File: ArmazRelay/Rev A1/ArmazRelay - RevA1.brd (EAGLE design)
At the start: 70 x 30 mm, 5 parts, among them J1 22-05-7028-02, J2 MSTBA3, K1 MY2

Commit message: Update board
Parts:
- added CC1: CC-BY-NC-SA, cc-by-sa:CC-BY-NC-SA
- added T1: EXMACHINA-LOGO-NAME, exmachina:EXM-LOGO-BASELINE
- moved H1 1.50 mm to (15.0, 15.0)
- moved H2 1.50 mm to (55.0, 15.0)
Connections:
- new net +24V: J2.1, K1.9
- new net GND: J1.2, J2.3, K1.14
- new net SIG_IN: J2.2, K1.13
- new net SIG_OUT: J1.1, K1.5
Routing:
- net SIG_OUT: track 0.00 -> 42.2 mm
- net SIG_IN: track 0.00 -> 37.1 mm
- added copper zone on layer 1, net +24V
- added copper zone on layer 16, net GND
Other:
- board text added: "ArmazRelay RevA1"
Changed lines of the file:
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@@
 <setting verticaltext="up"/>
 </settings>
-<grid distance="1" unitdist="mm" unit="mm" style="lines" multiple="1" display="no" altdistance="0.5" altunitdist="mm" altunit="mm"/>
+<grid distance="1" unitdist="mm" unit="mm" style="lines" multiple="1" display="no" altdistance="0.1" altunitdist="mm" altunit="mm"/>
 <layers>
 <layer number="1" name="Top" color="4" fill="1" visible="yes" active="yes"/>
@@
 <wire x1="67" y1="30" x2="3" y2="30" width="0" layer="20"/>
 <wire x1="3" y1="30" x2="0" y2="27" width="0" layer="20" curve="90"/>
+<dimension x1="15" y1="15" x2="55" y2="15" x3="35" y3="-7" textsize="2.54" layer="48"/>
+<dimension x1="35" y1="15" x2="0" y2="15" x3="17.5" y3="34" textsize="2.54" layer="48"/>
+<dimension x1="55.5" y1="15" x2="55.5" y2="30" x3="87" y3="22.5" textsize="2.54" layer="48"/>
+<dimension x1="67" y1="30" x2="58" y2="0" x3="95" y3="15" textsize="2.54" layer="48" dtype="vertical"/>
+<dimension x1="0" y1="3" x2="70" y2="4" x3="35" y3="-14" textsize="2.54" layer="48" dtype="horizontal"/>
+<text x="57.6" y="22.4" size="1.27" layer="21">ArmazRelay
+RevA1</text>
 </plain>
 <attributes>
@@
 </autorouter>
 <elements>
-<element name="H1" library="holes" package="3,0" value="MOUNT-HOLE3.0" x="13.5" y="15"/>
-<element name="H2" library="holes" package="3,0" value="MOUNT-HOLE3.0" x="56.5" y="15"/>
+<element name="H1" library="holes" package="3,0" value="MOUNT-HOLE3.0" x="15" y="15"/>
+<element name="H2" library="holes" package="3,0" value="MOUNT-HOLE3.0" x="55" y="15"/>
 <element name="J1" library="con-molex" package="7395-02" value="22-05-7028-02" x="65" y="15" rot="R90">
 <attribute name="OC_FARNELL" value="9731601" x="65" y="15" size="1.778" layer="27" rot="R90" display="off"/>
@@
 </element>
 <element name="K1" library="rel-omron" package="PY08" value="MY2" x="35" y="15" rot="R90"/>
+<element name="CC1" library="cc-by-sa" package="CC-BY-NC-SA" value="CC-BY-NC-SA" x="15" y="26"/>
+<element name="T1" library="exmachina" package="EXM-LOGO-BASELINE" value="EXMACHINA-LOGO-NAME" x="54" y="25"/>
 </elements>
 <signals>
+<signal name="+24V">
+<contactref element="J2" pad="1"/>
+<contactref element="K1" pad="9"/>
+<polygon width="0.4064" layer="1">
+<vertex x="-15" y="45"/>
+<vertex x="103" y="45"/>
+<vertex x="103" y="-21"/>
+<vertex x="-15" y="-21"/>
+</polygon>
+</signal>
+<signal name="GND">
+<contactref element="J2" pad="3"/>
+<contactref element="J1" pad="2"/>
+<contactref element="K1" pad="14"/>
+<polygon width="0.4064" layer="16">
+<vertex x="-13" y="43"/>
+<vertex x="101" y="43"/>
+<vertex x="101" y="25"/>
+<vertex x="101" y="-20"/>
+<vertex x="59" y="-20"/>
+<vertex x="-13" y="-20"/>
+</polygon>
+</signal>
+<signal name="SIG_IN">
+<contactref element="J2" pad="2"/>
+<contactref element="K1" pad="13"/>
+<wire x1="7.08" y1="15" x2="4" y2="15" width="0.4064" layer="1"/>
+<wire x1="4" y1="15" x2="3" y2="14" width="0.4064" layer="1"/>
+<wire x1="3" y1="14" x2="3" y2="6" width="0.4064" layer="1"/>
+<wire x1="3" y1="6" x2="4" y2="5" width="0.4064" layer="1"/>
+<wire x1="4" y1="5" x2="23" y2="5" width="0.4064" layer="1"/>
+<wire x1="23" y1="5" x2="24.75" y2="6.75" width="0.4064" layer="1"/>
+<wire x1="24.75" y1="6.75" x2="24.75" y2="8.5" width="0.4064" layer="1"/>
+</signal>
+<signal name="SIG_OUT">
+<contactref element="J1" pad="1"/>
+<contactref element="K1" pad="5"/>
+<wire x1="35.15" y1="8.5" x2="35.15" y2="5.85" width="0.4064" layer="1"/>
+<wire x1="35.15" y1="5.85" x2="36" y2="5" width="0.4064" layer="1"/>
+<wire x1="36" y1="5" x2="59" y2="5" width="0.4064" layer="1"/>
+<wire x1="59" y1="5" x2="61" y2="7" width="0.4064" layer="1"/>
+<wire x1="61" y1="7" x2="61" y2="15" width="0.4064" layer="1"/>
+<wire x1="61" y1="15" x2="62.27" y2="16.27" width="0.4064" layer="1"/>
+<wire x1="62.27" y1="16.27" x2="65" y2="16.27" width="0.4064" layer="1"/>
+</signal>
 </signals>
 </board>
 </drawing>
+<compatibility>
+<note version="6.3" minversion="6.2.2" severity="warning">
+Since Version 6.2.2 text objects can contain more than one line,
+which will not be processed correctly with this version.
+</note>
+</compatibility>
 </eagle>

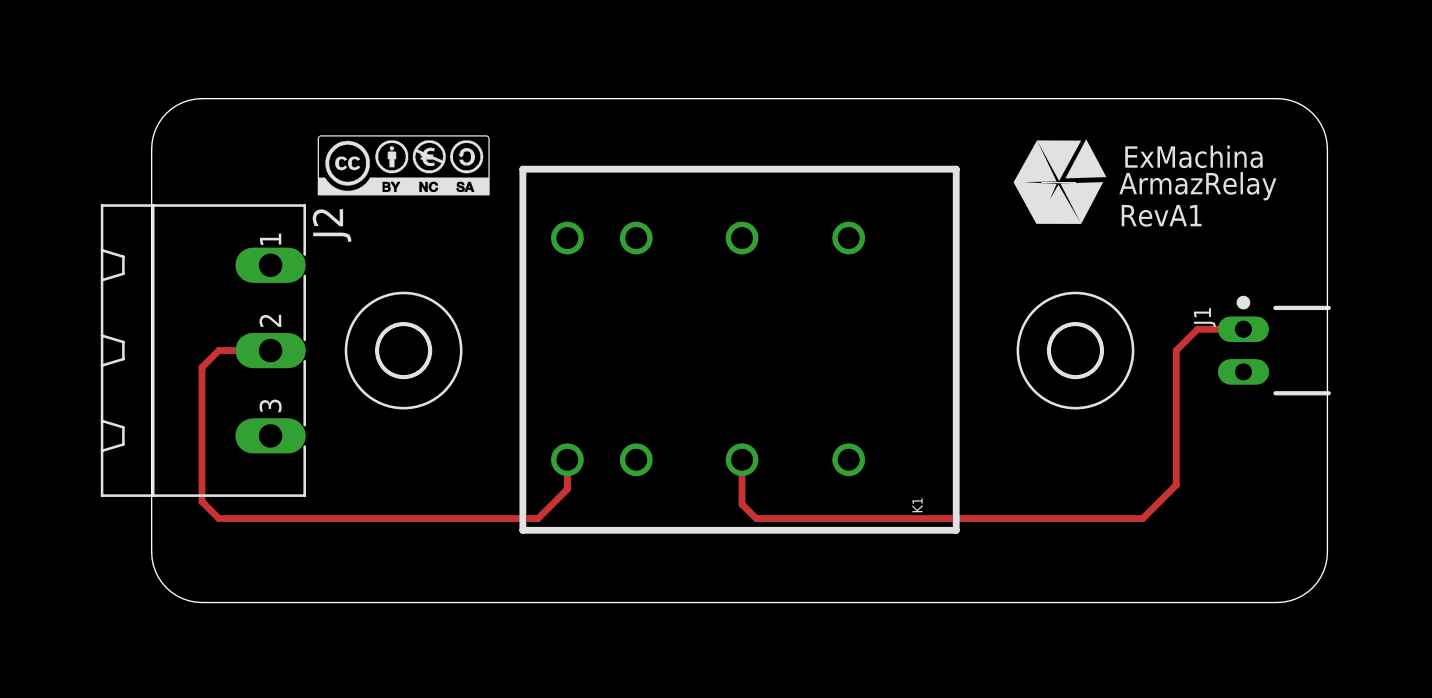
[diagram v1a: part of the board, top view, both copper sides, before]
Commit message: Add power connector and NC output
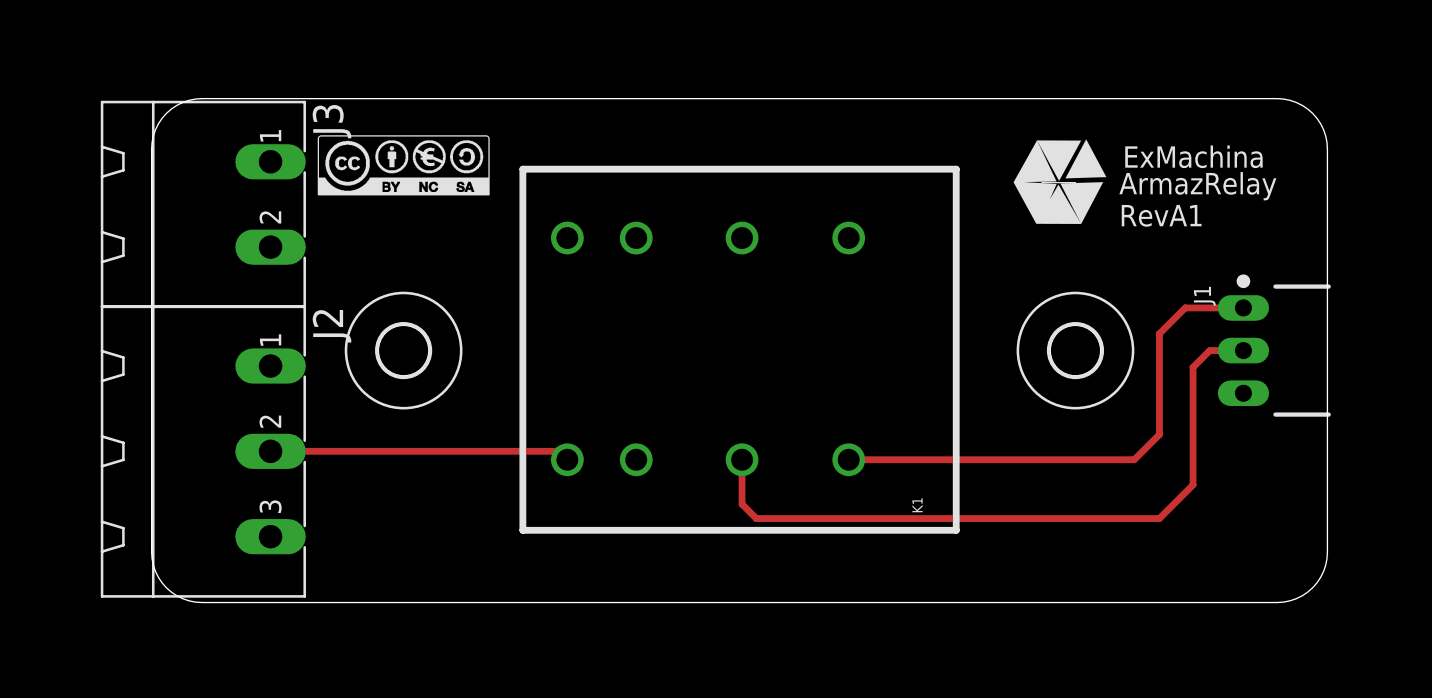
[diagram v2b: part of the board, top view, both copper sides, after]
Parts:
- added J3: MSTBA2, con-phoenix-508:MSTBA2
- J1: value 22-05-7028-02 -> 22-05-7038-03; device con-molex:7395-02 -> con-molex:7395-03
- moved J2 6.00 mm to (2.00, 9.00)
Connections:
- removed net SIG_OUT: J1.1, K1.5
- new net SIG_NC: J1.1, K1.1
- new net SIG_NO: J1.2, K1.5
- net +24V: now also J3.1
- net GND: now also J1.3, J3.2; no longer J1.2
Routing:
- net SIG_OUT: track 42.2 -> 0.00 mm
- net SIG_NO: track 0.00 -> 41.1 mm
- net SIG_NC: track 0.00 -> 30.8 mm
- net SIG_IN: track 37.1 -> 17.9 mm
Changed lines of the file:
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@@
 </class>
 </classes>
-<designrules name="default">
+<designrules name="default *">
 <description language="en">&lt;b&gt;EAGLE Design Rules&lt;/b&gt;
 &lt;p&gt;
@@
 <param name="dpGapFactor" value="2.5"/>
 <param name="checkGrid" value="0"/>
-<param name="checkAngle" value="0"/>
+<param name="checkAngle" value="1"/>
 <param name="checkFont" value="1"/>
 <param name="checkRestrict" value="1"/>
@@
 <element name="H1" library="holes" package="3,0" value="MOUNT-HOLE3.0" x="15" y="15"/>
 <element name="H2" library="holes" package="3,0" value="MOUNT-HOLE3.0" x="55" y="15"/>
-<element name="J1" library="con-molex" package="7395-02" value="22-05-7028-02" x="65" y="15" rot="R90">
-<attribute name="OC_FARNELL" value="9731601" x="65" y="15" size="1.778" layer="27" rot="R90" display="off"/>
-<attribute name="MPN" value="" x="65" y="15" size="1.778" layer="27" rot="R90" display="off"/>
-<attribute name="MF" value="" x="65" y="15" size="1.778" layer="27" rot="R90" display="off"/>
-<attribute name="OC_NEWARK" value="unknown" x="65" y="15" size="1.778" layer="27" rot="R90" display="off"/>
-</element>
-<element name="J2" library="con-phoenix-508" package="MSTBA3" value="MSTBA3" x="2" y="15" rot="R270">
-<attribute name="OC_FARNELL" value="3705183" x="2" y="15" size="1.778" layer="27" rot="R270" display="off"/>
-<attribute name="MPN" value="1757255" x="2" y="15" size="1.778" layer="27" rot="R270" display="off"/>
-<attribute name="MF" value="FARNELL" x="2" y="15" size="1.778" layer="27" rot="R270" display="off"/>
-<attribute name="OC_NEWARK" value="71C4162" x="2" y="15" size="1.778" layer="27" rot="R270" display="off"/>
+<element name="J2" library="con-phoenix-508" package="MSTBA3" value="MSTBA3" x="2" y="9" rot="R270">
+<attribute name="OC_FARNELL" value="3705183" x="2" y="9" size="1.778" layer="27" rot="R270" display="off"/>
+<attribute name="MPN" value="1757255" x="2" y="9" size="1.778" layer="27" rot="R270" display="off"/>
+<attribute name="MF" value="FARNELL" x="2" y="9" size="1.778" layer="27" rot="R270" display="off"/>
+<attribute name="OC_NEWARK" value="71C4162" x="2" y="9" size="1.778" layer="27" rot="R270" display="off"/>
 </element>
 <element name="K1" library="rel-omron" package="PY08" value="MY2" x="35" y="15" rot="R90"/>
 <element name="CC1" library="cc-by-sa" package="CC-BY-NC-SA" value="CC-BY-NC-SA" x="15" y="26"/>
 <element name="T1" library="exmachina" package="EXM-LOGO-BASELINE" value="EXMACHINA-LOGO-NAME" x="54" y="25"/>
+<element name="J3" library="con-phoenix-508" package="MSTBA2" value="MSTBA2" x="2" y="23.7" rot="R270">
+<attribute name="MF" value="FARNELL" x="2" y="23.7" size="1.778" layer="27" rot="R270" display="off"/>
+<attribute name="OC_NEWARK" value="71C4161" x="2" y="23.7" size="1.778" layer="27" rot="R270" display="off"/>
+<attribute name="OC_FARNELL" value="3705171" x="2" y="23.7" size="1.778" layer="27" rot="R270" display="off"/>
+<attribute name="MPN" value="1757242" x="2" y="23.7" size="1.778" layer="27" rot="R270" display="off"/>
+</element>
+<element name="J1" library="con-molex" package="7395-03" value="22-05-7038-03" x="65" y="15" rot="R90">
+<attribute name="MF" value="" x="65" y="15" size="1.778" layer="27" rot="R90" display="off"/>
+<attribute name="OC_NEWARK" value="unknown" x="65" y="15" size="1.778" layer="27" rot="R90" display="off"/>
+<attribute name="OC_FARNELL" value="9731610 " x="65" y="15" size="1.778" layer="27" rot="R90" display="off"/>
+<attribute name="MPN" value="" x="65" y="15" size="1.778" layer="27" rot="R90" display="off"/>
+</element>
 </elements>
 <signals>
@@
 <vertex x="-15" y="-21"/>
 </polygon>
+<contactref element="J3" pad="1"/>
 </signal>
 <signal name="GND">
 <contactref element="J2" pad="3"/>
-<contactref element="J1" pad="2"/>
 <contactref element="K1" pad="14"/>
 <polygon width="0.4064" layer="16">
@@
 <vertex x="-13" y="-20"/>
 </polygon>
+<contactref element="J3" pad="2"/>
+<contactref element="J1" pad="3"/>
 </signal>
 <signal name="SIG_IN">
 <contactref element="J2" pad="2"/>
 <contactref element="K1" pad="13"/>
-<wire x1="7.08" y1="15" x2="4" y2="15" width="0.4064" layer="1"/>
-<wire x1="4" y1="15" x2="3" y2="14" width="0.4064" layer="1"/>
-<wire x1="3" y1="14" x2="3" y2="6" width="0.4064" layer="1"/>
-<wire x1="3" y1="6" x2="4" y2="5" width="0.4064" layer="1"/>
-<wire x1="4" y1="5" x2="23" y2="5" width="0.4064" layer="1"/>
-<wire x1="23" y1="5" x2="24.75" y2="6.75" width="0.4064" layer="1"/>
-<wire x1="24.75" y1="6.75" x2="24.75" y2="8.5" width="0.4064" layer="1"/>
-</signal>
-<signal name="SIG_OUT">
-<contactref element="J1" pad="1"/>
+<wire x1="7.08" y1="9" x2="24.25" y2="9" width="0.4064" layer="1"/>
+<wire x1="24.25" y1="9" x2="24.75" y2="8.5" width="0.4064" layer="1"/>
+</signal>
+<signal name="SIG_NO">
 <contactref element="K1" pad="5"/>
 <wire x1="35.15" y1="8.5" x2="35.15" y2="5.85" width="0.4064" layer="1"/>
 <wire x1="35.15" y1="5.85" x2="36" y2="5" width="0.4064" layer="1"/>
-<wire x1="36" y1="5" x2="59" y2="5" width="0.4064" layer="1"/>
-<wire x1="59" y1="5" x2="61" y2="7" width="0.4064" layer="1"/>
-<wire x1="61" y1="7" x2="61" y2="15" width="0.4064" layer="1"/>
-<wire x1="61" y1="15" x2="62.27" y2="16.27" width="0.4064" layer="1"/>
-<wire x1="62.27" y1="16.27" x2="65" y2="16.27" width="0.4064" layer="1"/>
+<wire x1="36" y1="5" x2="60" y2="5" width="0.4064" layer="1"/>
+<wire x1="60" y1="5" x2="62" y2="7" width="0.4064" layer="1"/>
+<wire x1="62" y1="7" x2="62" y2="14" width="0.4064" layer="1"/>
+<contactref element="J1" pad="2"/>
+<wire x1="62" y1="14" x2="63" y2="15" width="0.4064" layer="1"/>
+<wire x1="63" y1="15" x2="65" y2="15" width="0.4064" layer="1"/>
+</signal>
+<signal name="SIG_NC">
+<contactref element="J1" pad="1"/>
+<contactref element="K1" pad="1"/>
+<wire x1="41.5" y1="8.5" x2="58.5" y2="8.5" width="0.4064" layer="1"/>
+<wire x1="58.5" y1="8.5" x2="60" y2="10" width="0.4064" layer="1"/>
+<wire x1="60" y1="10" x2="60" y2="16" width="0.4064" layer="1"/>
+<wire x1="60" y1="16" x2="61.54" y2="17.54" width="0.4064" layer="1"/>
+<wire x1="61.54" y1="17.54" x2="65" y2="17.54" width="0.4064" layer="1"/>
 </signal>
 </signals>

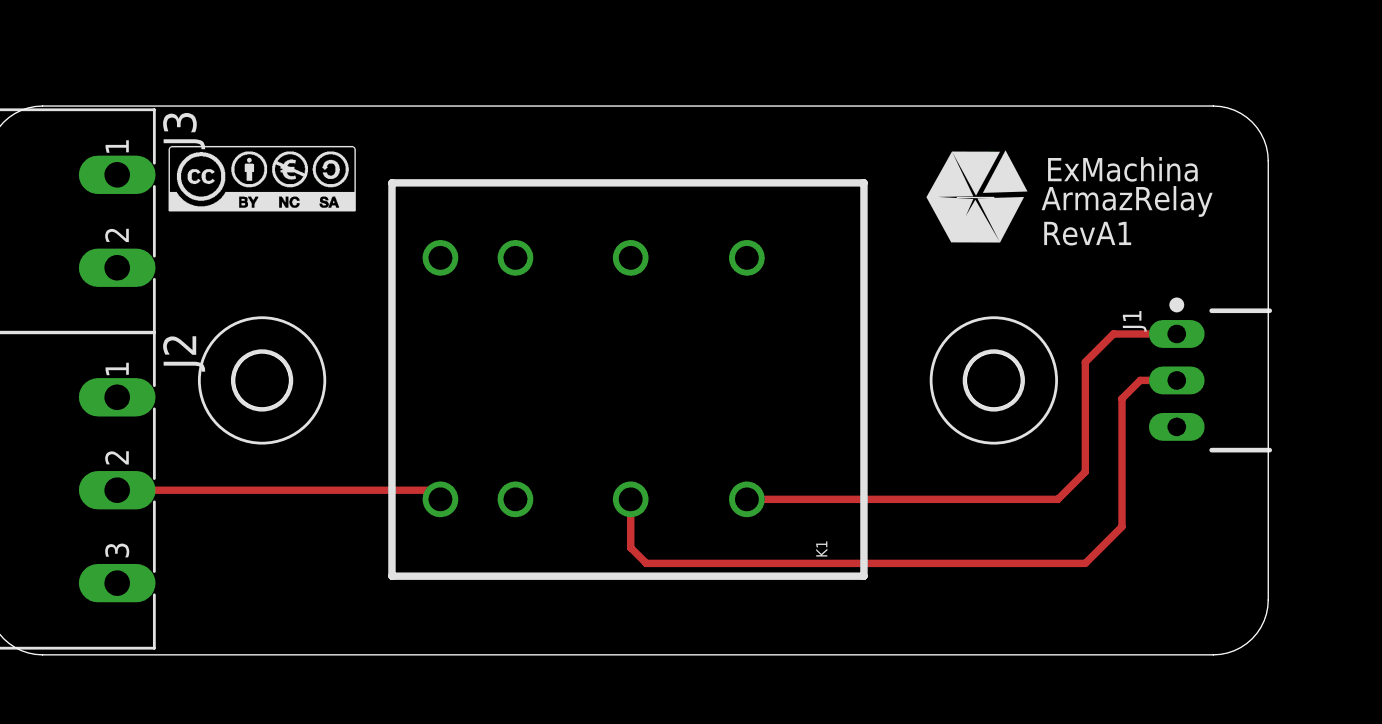
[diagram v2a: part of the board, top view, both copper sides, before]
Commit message: Final review of ArmazRelay board
- Add second output
- Change trace width to 32mil
- Add silkscreen labels
- Enlarge pad rings on the relay
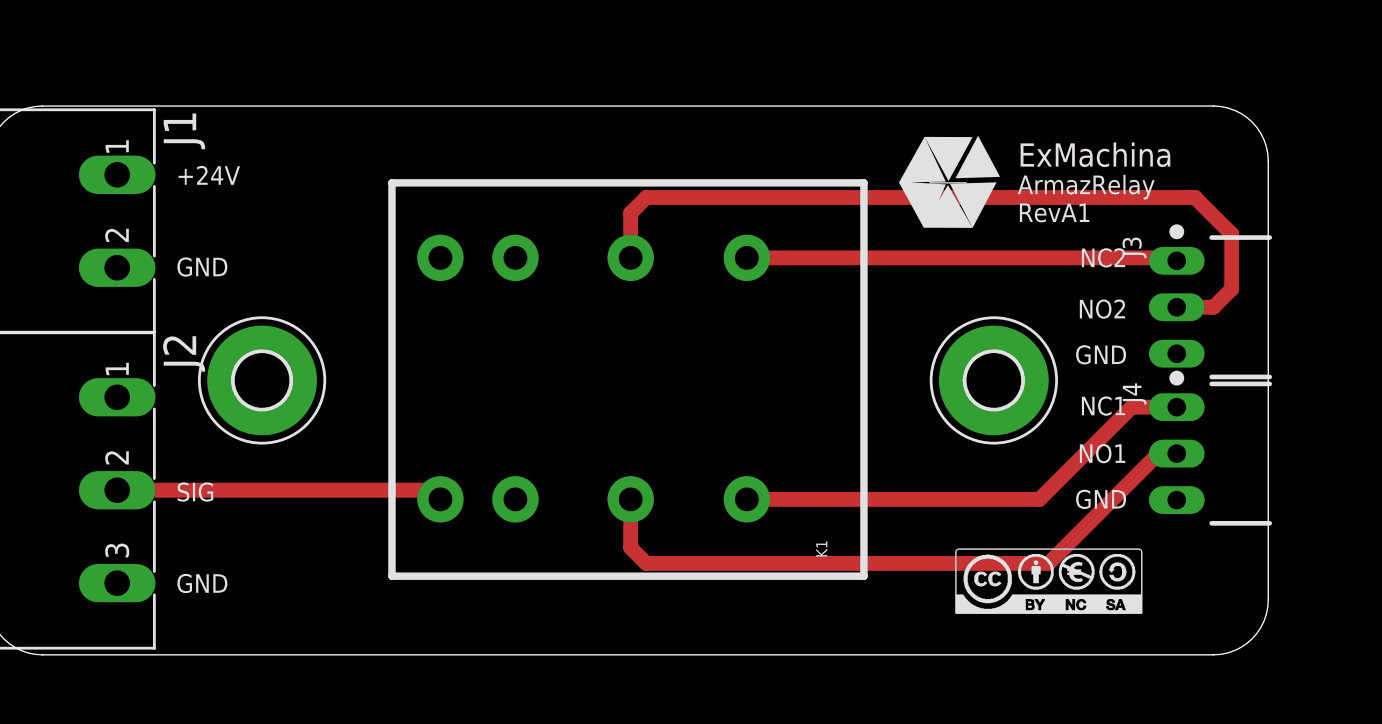
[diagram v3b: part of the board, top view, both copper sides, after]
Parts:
- added J4: 22-05-7038-03, con-molex:7395-03
- H1, H2: value MOUNT-HOLE3.0 -> MOUNT-PAD3,0; device holes:3,0 -> holes:P3,0
- J1: value 22-05-7038-03 -> MSTBA2; device con-molex:7395-03 -> con-phoenix-508:MSTBA2
- J3: value MSTBA2 -> 22-05-7038-03; device con-phoenix-508:MSTBA2 -> con-molex:7395-03
- moved J1 63.6 mm to (2.00, 23.7), turned to 270 degrees
- moved J3 63.2 mm to (65.0, 19.0), turned to 90 degrees
- moved CC1 48.3 mm to (58.0, 4.00)
- moved T1 1.70 mm to (52.5, 25.8)
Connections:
- removed net SIG_NC: J1.1, K1.1
- removed net SIG_NO: J1.2, K1.5
- new net SIG1_NC: J4.1, K1.1
- new net SIG1_NO: J4.2, K1.5
- new net SIG2_NC: J3.1, K1.4
- new net SIG2_NO: J3.2, K1.8
- net +24V: now also J1.1, K1.12; no longer J3.1
- net GND: now also J1.2, J3.3, J4.3; no longer J1.3, J3.2
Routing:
- net SIG2_NO: track 0.00 -> 42.9 mm
- net SIG_NO: track 41.1 -> 0.00 mm
- net SIG1_NO: track 0.00 -> 35.3 mm
- net SIG_NC: track 30.8 -> 0.00 mm
- net SIG1_NC: track 0.00 -> 25.6 mm
- net SIG2_NC: track 0.00 -> 23.6 mm
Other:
- board text added: "+24V"
- board text added: "GND"
- board text added: "NC1"
- board text added: "NC2"
- board text added: "NO1"
- board text added: "NO2"
- board text added: "SIG"
